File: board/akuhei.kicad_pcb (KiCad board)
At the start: 2 copper layers, 23 parts, among them J1 CLOCKPORT, J2 I2C, J3 AUXCLK, J4 JTAG, U1 XC9536XL-5VQG44C, U2 PCA9564, U3 TLV70233DBV

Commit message: Finishing touches...
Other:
- board outline added: 23.1 x 33 mm

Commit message: Move vias out of pads.
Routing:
- net /IA0: track 6.92 -> 13.2 mm
- net /IA1: track 5.73 -> 0.00 mm, vias 2 -> 0
- net I2C_RESET: track 4.78 -> 9.48 mm
- net LED: track 16.8 -> 20.0 mm
- net I2C_INT: track 8.94 -> 11.0 mm
- net /D7: track 32.0 -> 33.9 mm
- net AUXCLK: track 15.5 -> 16.2 mm, vias 1 -> 0
- net SDA: track 10.8 -> 11.4 mm
- net +3V3: track 84.0 -> 83.9 mm, vias 6 -> 5

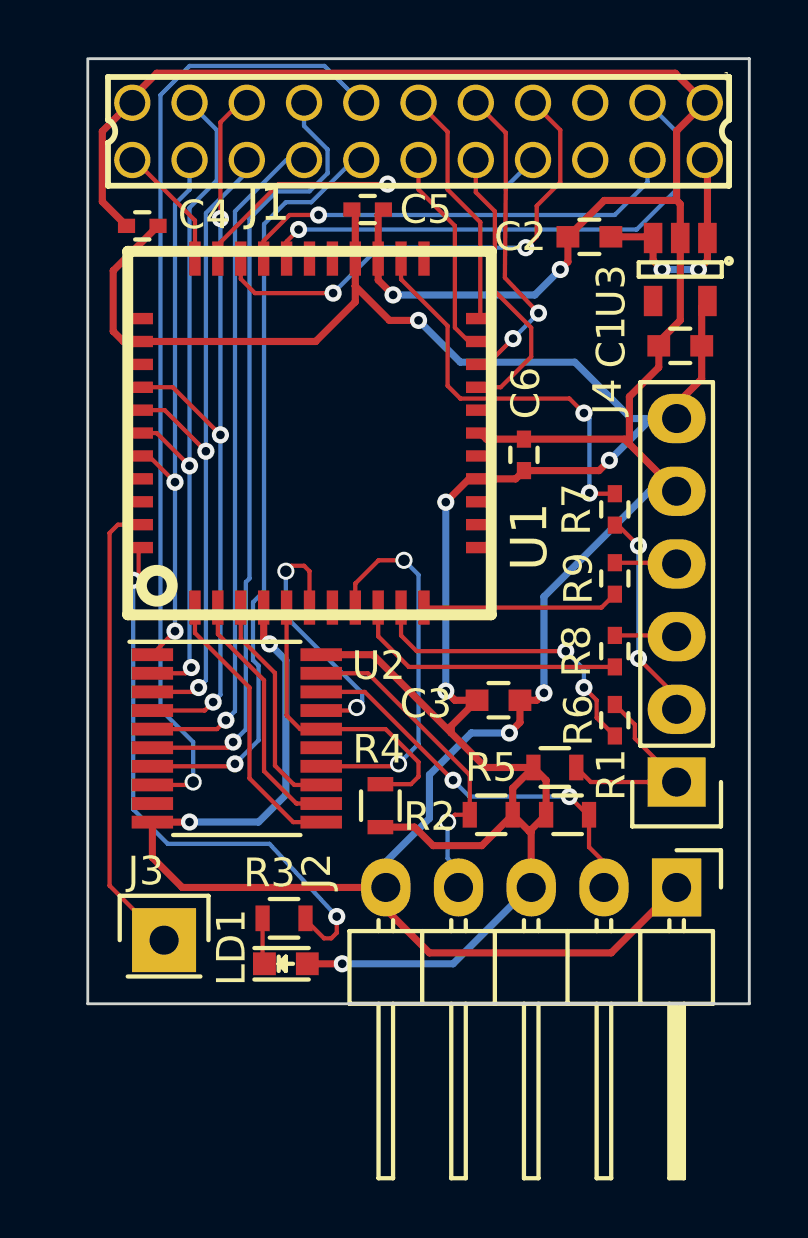
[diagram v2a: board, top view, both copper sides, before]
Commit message: Add no-CPLD version.
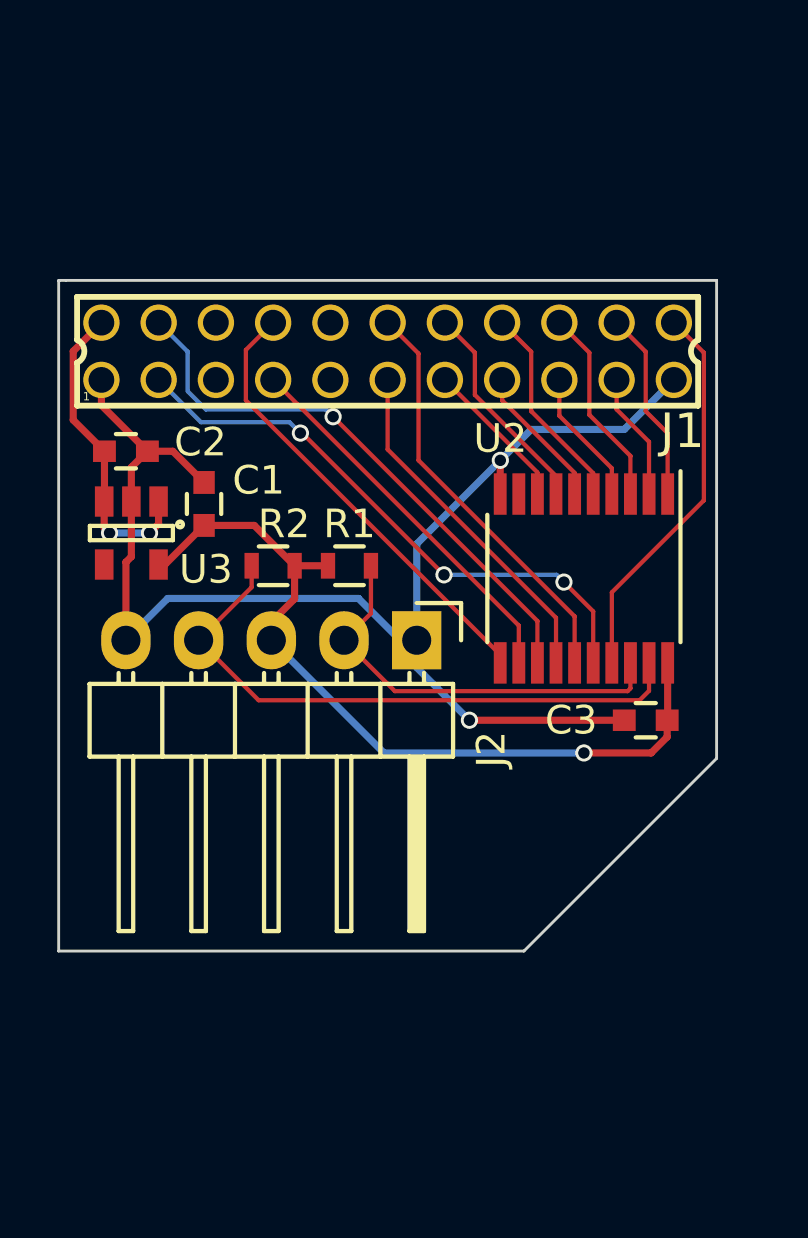
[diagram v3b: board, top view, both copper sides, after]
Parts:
- removed C4, C5, C6: 0.1uF, Capacitors_SMD:C_0402
- removed J3: AUXCLK, Pin_Headers:Pin_Header_Straight_1x01
- removed J4: JTAG, Pin_Headers:Pin_Header_Straight_1x06
- removed LD1: LED, LEDs:LED-0603
- removed R3: 220, Resistors_SMD:R_0603
- removed R4: 4.7k, Resistors_SMD:R_0603
- removed R5: 10k, Resistors_SMD:R_0603
- removed R6, R7, R8, R9: 220, Capacitors_SMD:C_0402
- removed U1: XC9536XL-5VQG44C, VQFP44
- moved U3 21.3 mm to (139.2, 105.5)
- moved C2 17.8 mm to (139.0, 102.6), turned to 0 degrees
- moved C1 17.5 mm to (141.7, 104.5), turned to 90 degrees
- moved U2 13.4 mm to (155.0, 107.1), turned to 270 degrees
- moved J2 12.5 mm to (149.2, 109.2)
- moved R1 11.6 mm to (146.8, 106.6)
- moved R2 11.6 mm to (144.1, 106.6)
- moved J1 7.76 mm to (148.1, 99.1), turned to 0 degrees
- moved C3 5.19 mm to (157.2, 112.0), turned to 180 degrees
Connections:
- J1 pad 10: /A4 -> Net-(J1-Pad10)
- J1 pad 9: /A3 -> Net-(J1-Pad9)
- U2 pad 11: I2C_WR -> CP_IOWR
- U2 pad 12: I2C_RD -> CP_IORD
- U2 pad 13: I2C_CE -> CP_CS
- U2 pad 14: /IA0 -> /A1
- U2 pad 15: /IA1 -> /A2
- U2 pad 16: I2C_INT -> CP_INT
- U2 pad 17: I2C_RESET -> CP_RESET
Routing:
- net GND: track 115.9 -> 48.7 mm, vias 6 -> 2
- net +3V3: track 83.9 -> 28.3 mm, vias 5 -> 1
- net /D7: track 33.9 -> 5.33 mm, vias 1 -> 0
- net /D3: track 27.4 -> 4.75 mm, vias 3 -> 0
- net /D5: track 27.6 -> 5.04 mm, vias 1 -> 0
- net LED: track 20.0 -> 0.00 mm, vias 2 -> 0
- net /D1: track 24.2 -> 4.46 mm, vias 2 -> 0
- net /D6: track 26.7 -> 7.60 mm, vias 1 -> 0
- net /D2: track 23.8 -> 7.02 mm, vias 2 -> 0
- net /D4: track 23.8 -> 7.31 mm, vias 1 -> 0
- net AUXCLK: track 16.2 -> 0.00 mm
- net TDO: track 14.0 -> 0.00 mm, vias 2 -> 0
- net /IA0: track 13.2 -> 0.00 mm, vias 2 -> 0
- net /D0: track 19.5 -> 6.73 mm, vias 2 -> 0
- net /A3: track 11.0 -> 0.00 mm, vias 2 -> 0
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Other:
- board size 23.1 x 33 mm -> 23 x 23.4 mm
- board text added: "Akuhei rev1"
- board text added: "Sakura"
